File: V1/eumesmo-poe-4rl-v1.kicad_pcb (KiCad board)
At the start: 4 copper layers, 99.5 x 45 mm, 121 parts, among them J1 USB_C_Receptacle_USB2.0, J2 RJ45 JACK, J3 250-202, J4 250-202, J5 250-202, J6 250-202, K1 G5NB-1A-E-DC5, K2 G5NB-1A-E-DC5, K3 G5NB-1A-E-DC5, K4 G5NB-1A-E-DC5, Q1 UMH3N, Q2 WPM2015-3/TR, Q3 LMUN2211LT1G, Q4 MMBT2222A, Q5 MMBT2222A, Q6 MMBT2222A, Q7 MMBT2222A, SW1 RESET, U1 CH340K, U2 ESP32-WROOM-32UE-N16, U3 LAN8710A, U4 TPS2376DDAR-H, U5 TX4138, U6 SY8089A1AAC

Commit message: Rerouted TX/RX pairs between magjack and PHY.
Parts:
- moved D2 1.35 mm to (146.2, 94.0)
- moved R16 0.79 mm to (138.2, 95.0)
- moved R18 0.79 mm to (138.2, 93.5)
- moved R19 0.79 mm to (138.2, 92.5)
- moved R20 0.79 mm to (138.2, 91.5)
- moved C12 0.56 mm to (140.8, 91.5)
- moved C15 0.25 mm to (134.0, 95.0)
- moved C9 0.25 mm to (147.5, 89.5)
- moved R17 0.25 mm to (147.5, 90.5)
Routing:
- net /ETHRXD-: track 21.7 -> 27.7 mm, vias 2 -> 0
- net 5VUSB: track 73.8 -> 69.0 mm
- net /ETHRXD+: track 25.1 -> 28.1 mm
- net +3V3A: track 48.6 -> 46.6 mm, vias 7 -> 6
- net /ETHTXD+: track 20.8 -> 18.9 mm
- net /ETHTXD-: track 20.8 -> 19.6 mm, vias 2 -> 1
- net GND: track 73.1 -> 72.2 mm, vias 58 -> 56
- net /ETHLEDYK: track 13.8 -> 13.1 mm
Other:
- board text added: "V1.0.0 2026-06-16"
- board text removed: "V1.0.0 2026-06-15"

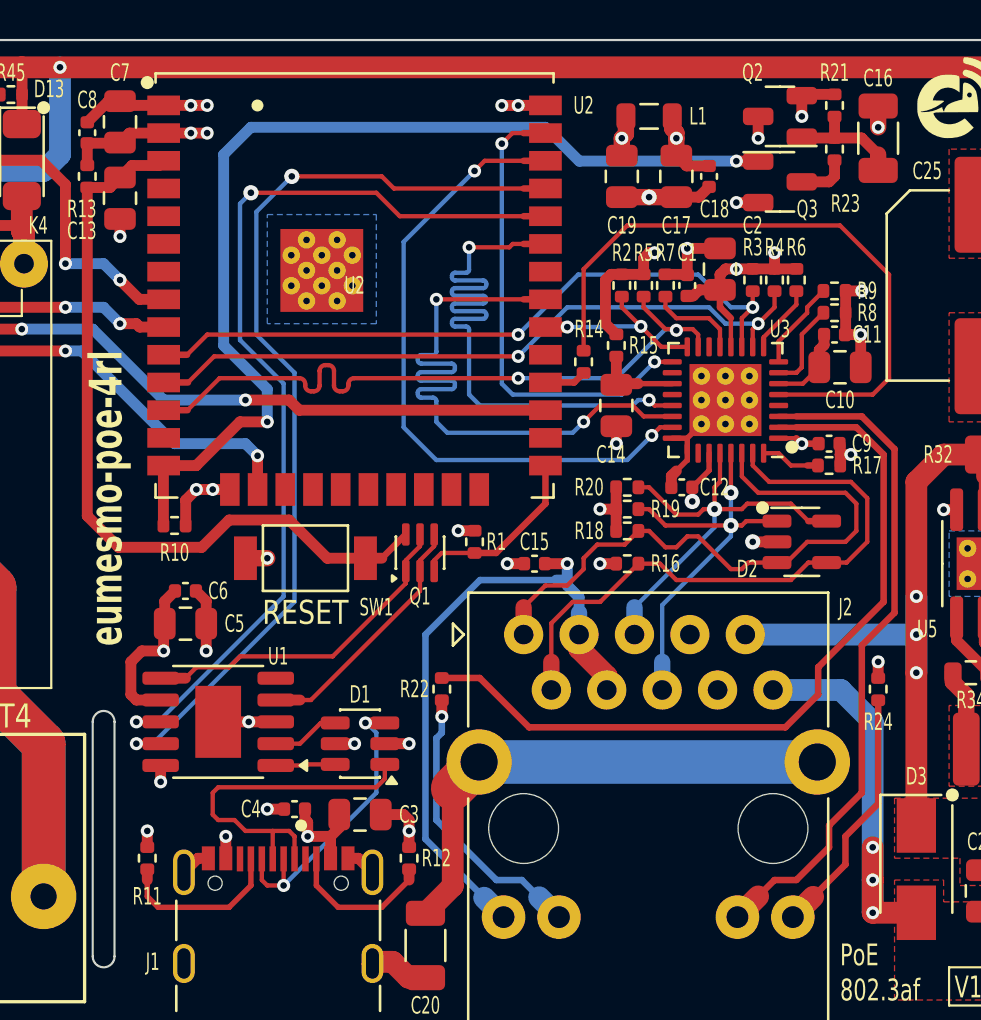
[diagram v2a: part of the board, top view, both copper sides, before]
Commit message: Widened pads at tracks and vias.
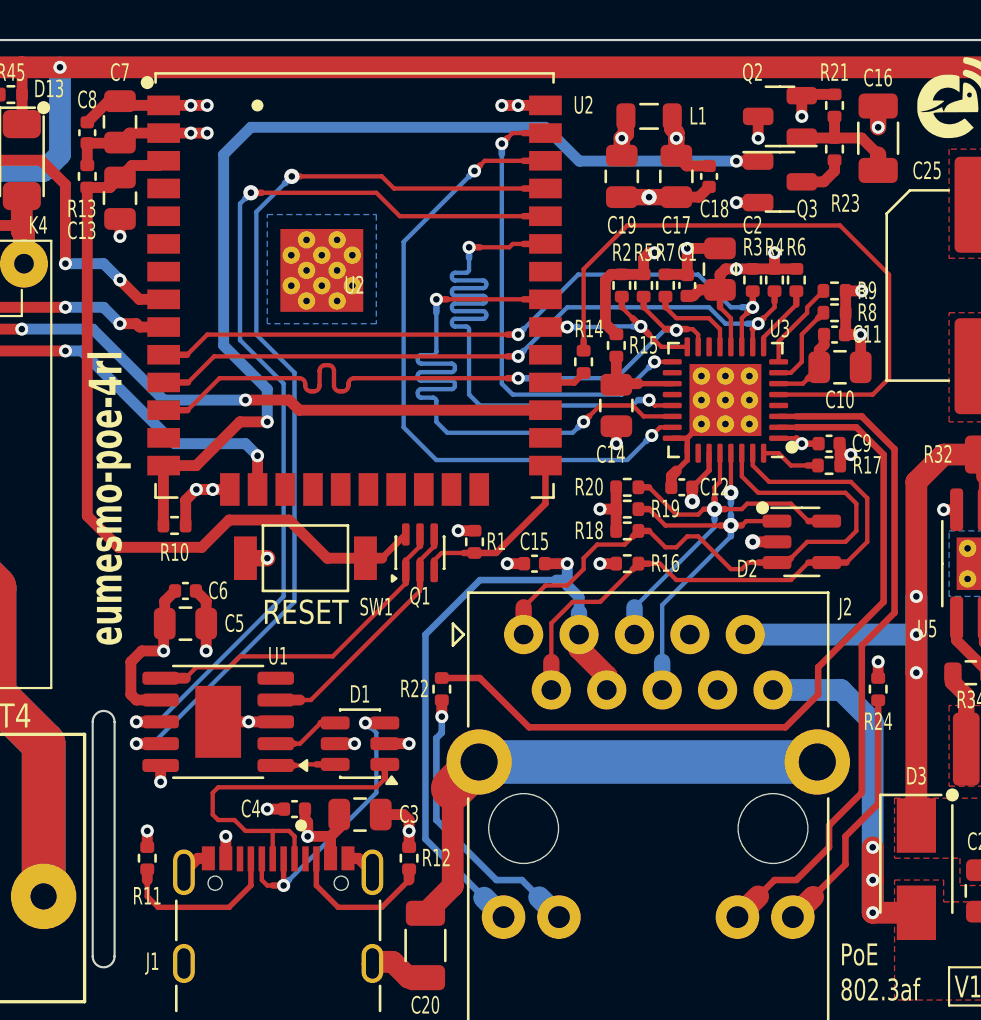
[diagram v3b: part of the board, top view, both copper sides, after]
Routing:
- net +3V3A: track 46.6 -> 47.2 mm

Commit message: Release V1.0.0
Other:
- board text added: "V1.0.0 2026-06-17"
- board text removed: "V1.0.0 2026-06-16"
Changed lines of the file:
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@@
 	(title_block
 		(title "eumesmo 4x Relay Output Module with PoE")
-		(date "2026-06-16")
+		(date "2026-06-17")
 		(rev "V1.0")
 	)
@@
 		)
 	)
-	(gr_text "V1.0.0 2026-06-16"
+	(gr_text "V1.0.0 2026-06-17"
 		(at 153.25 115 0)
 		(layer "F.SilkS")

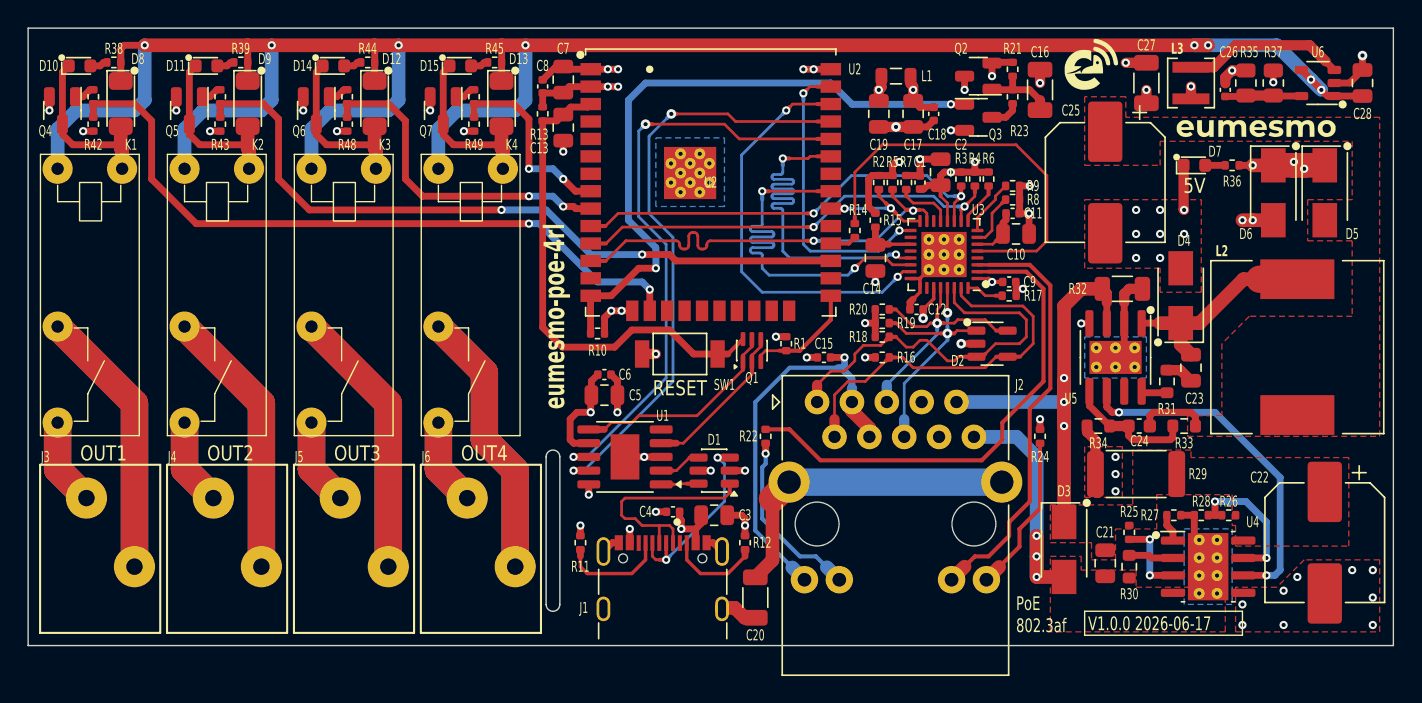
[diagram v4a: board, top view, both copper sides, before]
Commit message: Added CPU health LED
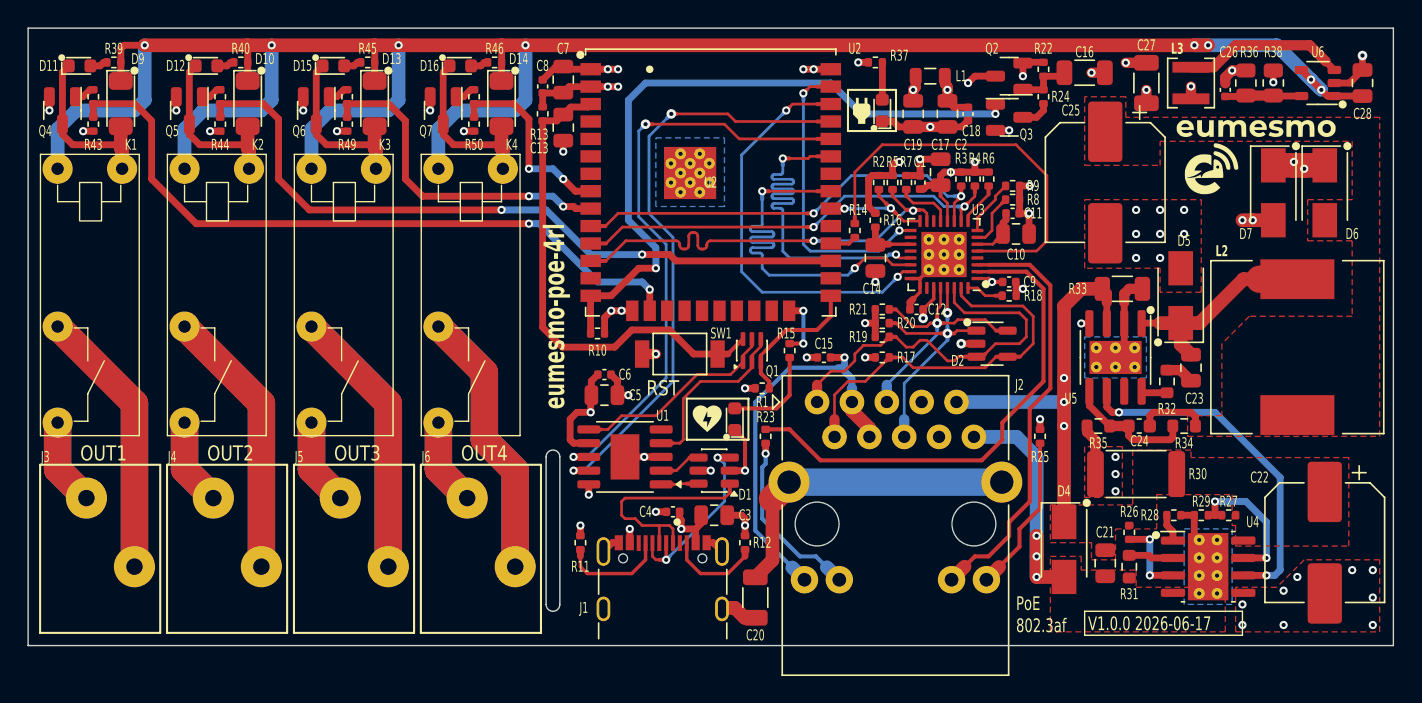
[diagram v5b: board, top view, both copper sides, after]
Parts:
- removed the D7 at (161.0, 81.0)
- removed the R36 at (163.8, 81.0)
- added D3: WHITE/0603, Tales:LED_0603_1608Metric, F.Cu at (127.5, 99.5)
- added D8: WHITE, Tales:LED_0603_1608Metric, F.Cu at (138.2, 77.0)
- added R15: 300R, Tales:R_0402_1005Metric, F.Cu at (131.5, 94.5)
- added R37: 300R, Tales:R_0402_1005Metric, F.Cu at (137.8, 73.5)
- added REF**: Icon_Heart_Flash, Tales:Icon_Heart_Flash, F.Cu at (125.5, 99.5)
- added REF**: Icon_Power_Plug, Tales:Icon_Power_Plug, F.Cu at (136.8, 77.0)
- moved G*** 11.6 mm to (162.3, 82.1)
- moved R1 3.69 mm to (129.5, 97.2), turned to 0 degrees
- moved C16 3.48 mm to (153.0, 74.2), turned to 180 degrees
- moved C17 2.50 mm to (143.0, 77.2)
- moved C18 2.50 mm to (144.5, 77.2)
- moved C19 2.50 mm to (140.5, 77.2)
- moved L1 2.50 mm to (141.8, 74.5)
- moved Q2 2.25 mm to (147.5, 74.5)
- moved Q3 2.25 mm to (147.5, 77.5)
- moved R22 2.25 mm to (150.0, 74.0)
- moved R24 2.25 mm to (150.0, 76.0)
- renumbered D9 to D10, D10 to D11, D11 to D12, D12 to D13, D13 to D14, D14 to D15, D15 to D16, D3 to D4, D4 to D5, D5 to D6, D6 to D7, D8 to D9, R15 to R16, R16 to R17, R17 to R18, R18 to R19, R19 to R20, R20 to R21, R21 to R22, R22 to R23, R23 to R24, R24 to R25, R25 to R26, R26 to R27, R27 to R28, R28 to R29, R29 to R30, R30 to R31, R31 to R32, R32 to R33, R33 to R34, R34 to R35, R35 to R36, R37 to R38, R38 to R39, R39 to R40, R40 to R41, R41 to R42, R42 to R43, R43 to R44, R44 to R45, R45 to R46, R46 to R47, R47 to R48, R48 to R49, R49 to R50
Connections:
- U2 pad 24: unconnected-(U2-IO2-Pad24) -> /CPUOK
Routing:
- net /CPULED: track 0.00 -> 7.14 mm
- net /CPUOK: track 0.00 -> 4.27 mm, vias 0 -> 2
- net PHYPWR: track 47.1 -> 50.3 mm
- net /POWER/3V3LED: track 0.00 -> 2.72 mm
- net +5V: track 168.0 -> 165.5 mm, vias 11 -> 10
- net /ESPPROG: track 8.52 -> 10.5 mm
- net GND: track 72.2 -> 74.2 mm
- net /UARTNDTR: track 11.7 -> 13.1 mm
- net /POWER/PWRON: track 1.45 -> 0.00 mm
- net /PHYPWRFET: track 5.48 -> 4.07 mm
- net +3V3LAN: track 19.9 -> 21.2 mm
- net +3V3: track 39.9 -> 38.8 mm, vias 10 -> 11
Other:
- board text added: "RST"
- board text removed: "5V"
- board text removed: "RESET"
